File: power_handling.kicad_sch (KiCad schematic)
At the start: 57 parts, among them J2 usb_c, SW1 SMXS_01K_TP, U1 TPS62130, U12 FSUSB42MUX, U13 AP22802AW5-7, U2 MIC5365-1.8YC5-TR, U3 TPS62130, U4 TPS7A0309PDBVR

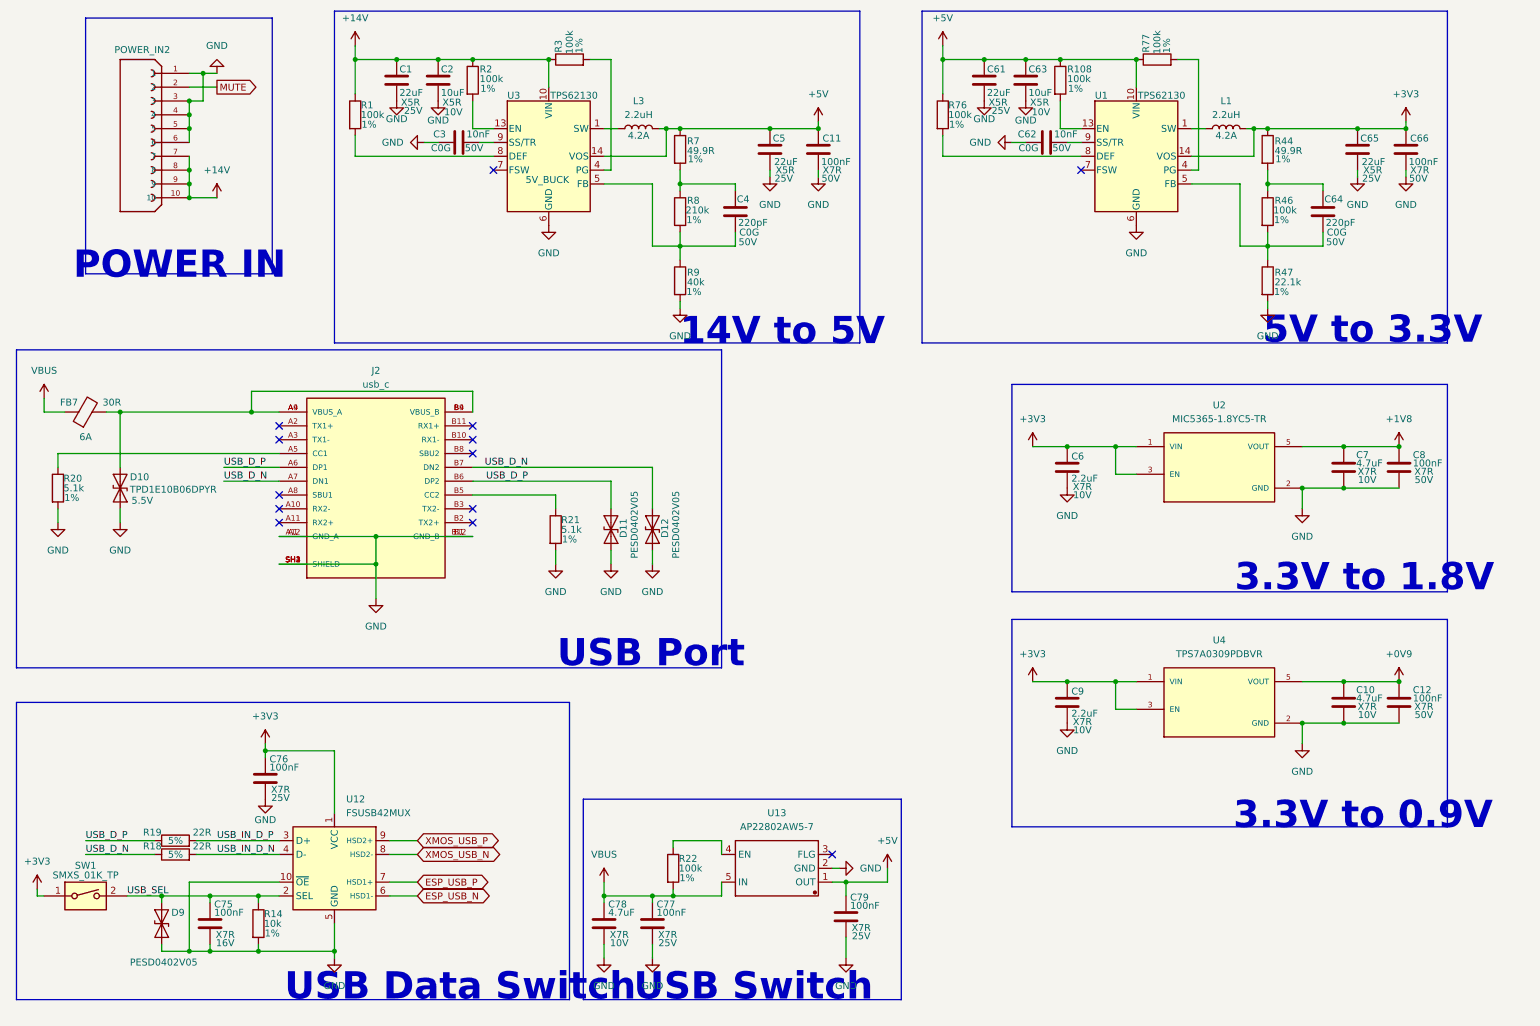
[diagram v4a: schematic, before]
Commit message: modifications for manufacturing
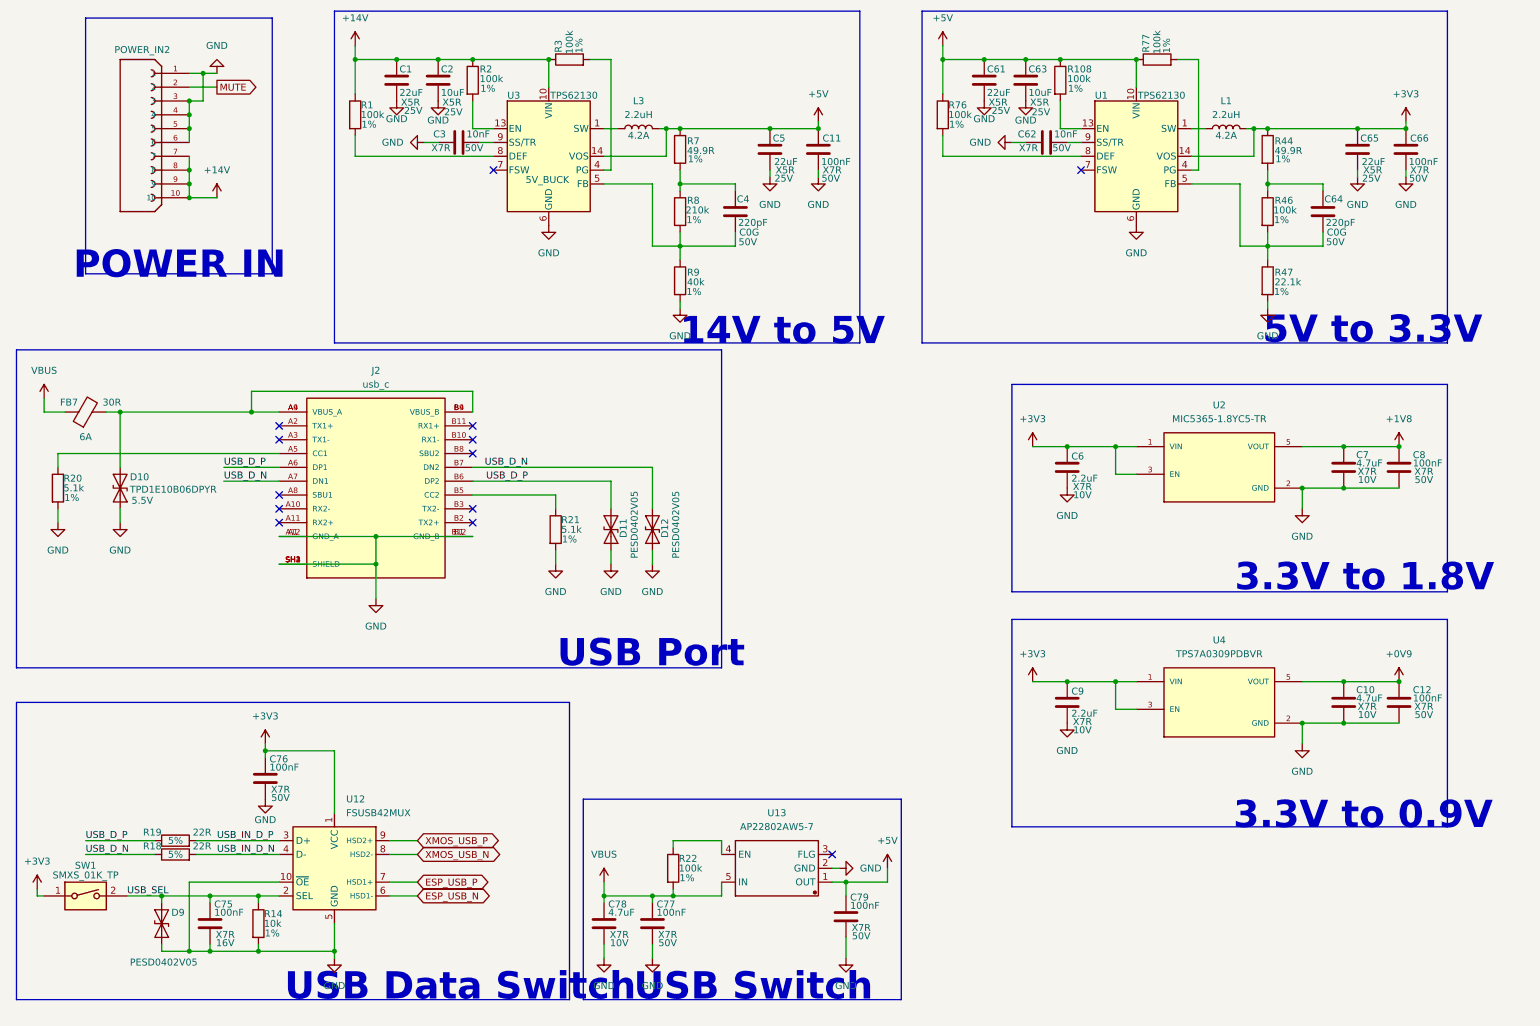
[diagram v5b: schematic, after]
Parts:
- C1, C5, C61, C65: Manufacturer (none) -> Samsung Electro-Mechanics; Manufacturer Part (none) -> CL21A226MAQNNNE
- C10, C7, C78: Manufacturer (none) -> Murata Electronics; Manufacturer Part (none) -> GRM188Z71A475KE15D
- C11, C12, C66, C8: Manufacturer (none) -> YAGEO; Manufacturer Part (none) -> CC0805KRX7R9BB104
- C2, C63: Manufacturer (none) -> Samsung Electro-Mechanics; Manufacturer Part (none) -> CL21A106KAYNNNE; Voltage 10V -> 25V
- C3, C62: Dielectric C0G -> X7R; Manufacturer (none) -> Samsung Electro-Mechanics; Manufacturer Part (none) -> CL05B103KB5NNNC
- C4, C64: Manufacturer (none) -> FH (Guangdong Fenghua Advanced Tech); Manufacturer Part (none) -> 0603CG221J500NT
- C6, C9: Manufacturer (none) -> Murata Electronics; Manufacturer Part (none) -> GRM188R71A225KE15D
- C75: Manufacturer (none) -> Samsung Electro-Mechanics; Manufacturer Part (none) -> CL05B104KO5NNNC
- C76, C77, C79: Manufacturer (none) -> YAGEO; Manufacturer Part (none) -> CC0603KRX7R9BB104; Voltage 25V -> 50V
- R1, R108, R2, R22, R3, R76, R77: Manufacturer (none) -> UNI-ROYAL(Uniroyal Elec); Manufacturer Part (none) -> 0402WGJ0104TCE
- R14: Manufacturer (none) -> UNI-ROYAL(Uniroyal Elec); Manufacturer Part (none) -> 0402WGF1002TCE
- R18, R19: Manufacturer (none) -> UNI-ROYAL(Uniroyal Elec); Manufacturer Part (none) -> 0402WGF220JTCE
- R20, R21: Manufacturer (none) -> UNI-ROYAL(Uniroyal Elec); Manufacturer Part (none) -> 0402WGF5101TCE
- R44, R7: Manufacturer (none) -> UNI-ROYAL(Uniroyal Elec); Manufacturer Part (none) -> 0603WAF499JT5E
- R46: Manufacturer (none) -> UNI-ROYAL(Uniroyal Elec); Manufacturer Part (none) -> 0603WAF1003T5E
- R47: Manufacturer (none) -> UNI-ROYAL(Uniroyal Elec); Manufacturer Part (none) -> 0603WAF2212T5E
- R8: Manufacturer (none) -> UNI-ROYAL(Uniroyal Elec); Manufacturer Part (none) -> 0603WAF2103T5E
- R9: Manufacturer (none) -> VO; Manufacturer Part (none) -> SCR0603F40K

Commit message: modifications for manufacturing
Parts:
- C1, C5, C61, C65: LCSC Part # (none) -> C45783
- C10, C7, C78: LCSC Part # (none) -> C913474
- C11, C12, C66, C8: LCSC Part # (none) -> C49678
- C2, C63: LCSC Part # (none) -> C15850
- C3, C62: LCSC Part # (none) -> C15195
- C4, C64: LCSC Part # (none) -> C156398
- C6, C9: LCSC Part # (none) -> C86018
- C75: LCSC Part # (none) -> C1525
- C76, C77, C79: LCSC Part # (none) -> C14663
- D10: LCSC Part # (none) -> C48260
- D11, D12, D9: LCSC Part # (none) -> C19626254
- FB7: LCSC Part # (none) -> C17305
- J2: LCSC Part # (none) -> C134092
- L1, L3: LCSC Part # (none) -> C719179
- POWER_IN2: LCSC Part # (none) -> C324723
- R1, R108, R2, R22, R3, R76, R77: LCSC Part # (none) -> C25530
- R14: LCSC Part # (none) -> C25744
- R18, R19: LCSC Part # (none) -> C25092
- R20, R21: LCSC Part # (none) -> C25905
- R44, R7: LCSC Part # (none) -> C23185
- R46: LCSC Part # (none) -> C25803
- R47: LCSC Part # (none) -> C25961
- R8: LCSC Part # (none) -> C22952
- R9: LCSC Part # (none) -> C3016445
- SW1: LCSC Part # (none) -> C5439760
- U1, U3: LCSC Part # (none) -> C337502
- U12: LCSC Part # (none) -> C11355
- U13: LCSC Part # (none) -> C211404
- U2: LCSC Part # (none) -> C626087
- U4: LCSC Part # (none) -> C2977167

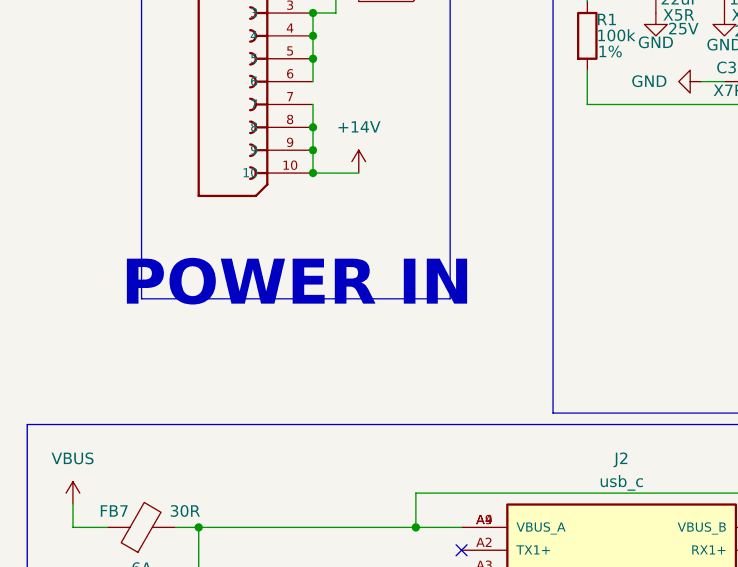
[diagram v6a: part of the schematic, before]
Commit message: modifications for manufacturing
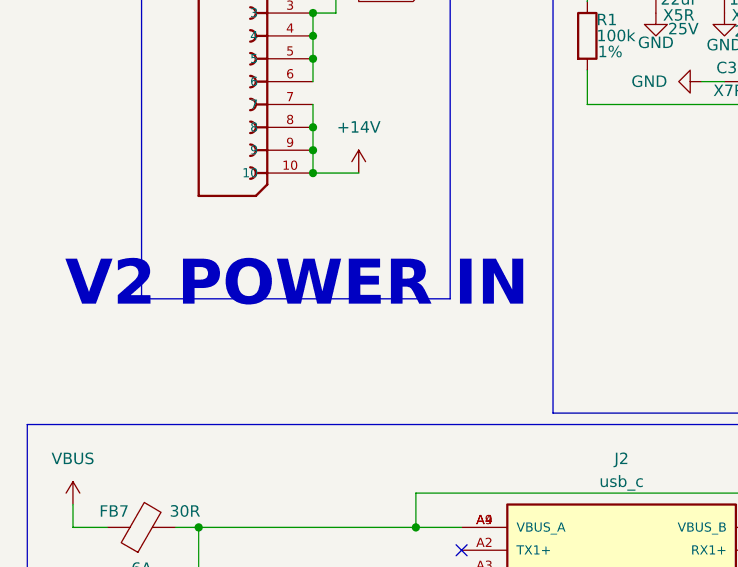
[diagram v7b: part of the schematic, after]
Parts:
- FB7: footprint Onju:TPD1E05U06DPYR -> Resistor_SMD:R_0603_1608Metric
- L1, L3: footprint Inductor_SMD:L_Coilcraft_XxL4020 -> Inductor_SMD:L_Cenker_CKCS4020
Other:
- note added: "V2 POWER IN"
- note removed: "POWER IN"
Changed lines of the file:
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@@
 		)
 	)
-	(text "POWER IN"
+	(text "V2 POWER IN"
 		(exclude_from_sim no)
 		(at 42.672 60.706 0)
@@
 			)
 		)
-		(property "Footprint" "Inductor_SMD:L_Coilcraft_XxL4020"
+		(property "Footprint" "Inductor_SMD:L_Cenker_CKCS4020"
 			(at 127 35.56 0)
 			(effects
@@
 			)
 		)
-		(property "Footprint" "Onju:TPD1E05U06DPYR"
+		(property "Footprint" "Resistor_SMD:R_0603_1608Metric"
 			(at 25.4 89.408 90)
 			(effects
@@
 			)
 		)
-		(property "Footprint" "Inductor_SMD:L_Coilcraft_XxL4020"
+		(property "Footprint" "Inductor_SMD:L_Cenker_CKCS4020"
 			(at 234.95 35.56 0)
 			(effects

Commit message: fixing errors
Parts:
- R46: value 100k -> 68.1k; LCSC Part # C25803 -> C25976; Manufacturer Part 0603WAF1003T5E -> 0603WAF6812T5E; Supplier Part C25803 -> C25976
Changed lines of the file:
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@@
 			)
 		)
-		(property "Value" "100k"
+		(property "Value" "68.1k"
 			(at 243.586 50.546 0)
 			(effects
@@
 			)
 		)
-		(property "Supplier Part" "C25803"
+		(property "Supplier Part" "C25976"
 			(at 242.57 50.8 0)
 			(effects
@@
 			)
 		)
-		(property "Manufacturer Part" "0603WAF1003T5E"
+		(property "Manufacturer Part" "0603WAF6812T5E"
 			(at 242.57 50.8 0)
 			(effects
@@
 			)
 		)
-		(property "LCSC Part #" "C25803"
+		(property "LCSC Part #" "C25976"
 			(at 242.57 50.8 0)
 			(effects
